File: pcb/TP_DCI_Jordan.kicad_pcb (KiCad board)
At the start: 2 copper layers, 50 x 30 mm, 19 parts, among them J1 MICRO, J2 Display, SW1 SW_DIP_x03, U1 PCF8574

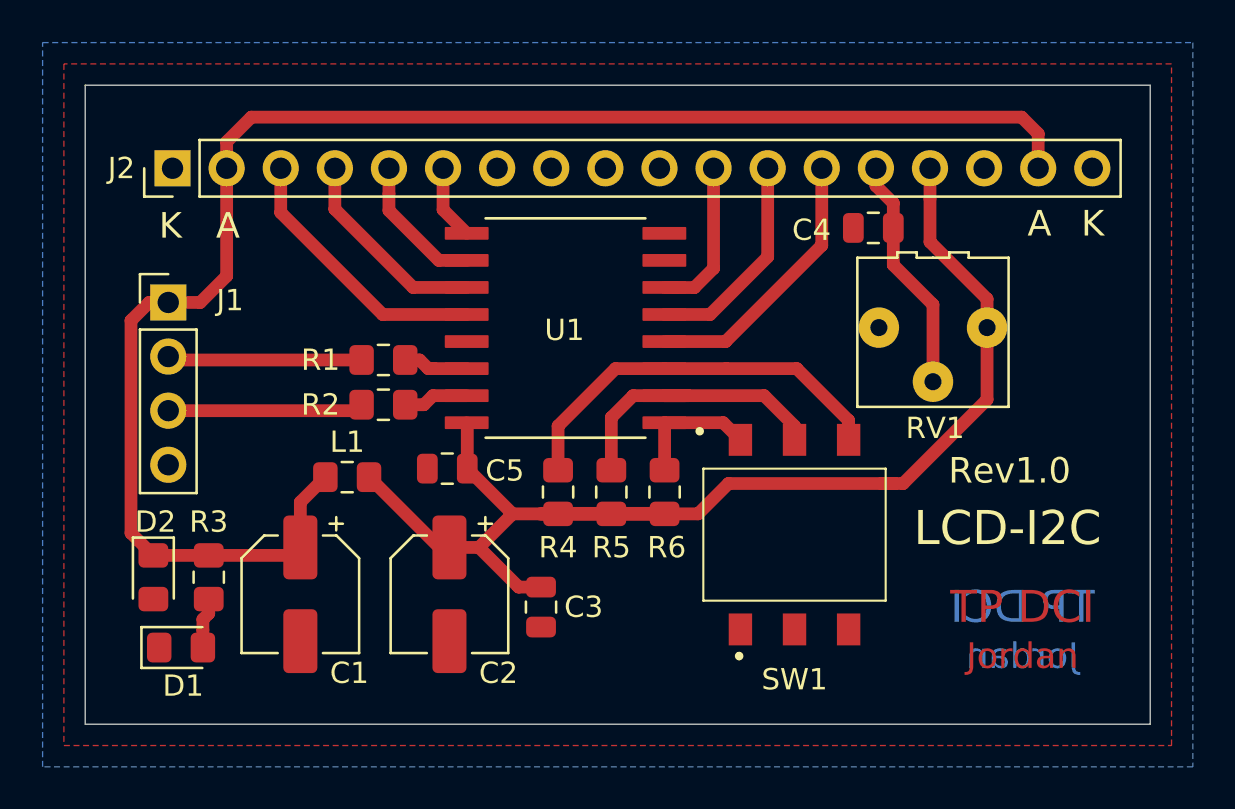
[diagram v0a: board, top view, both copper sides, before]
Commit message: actualización de KiCAD6.0
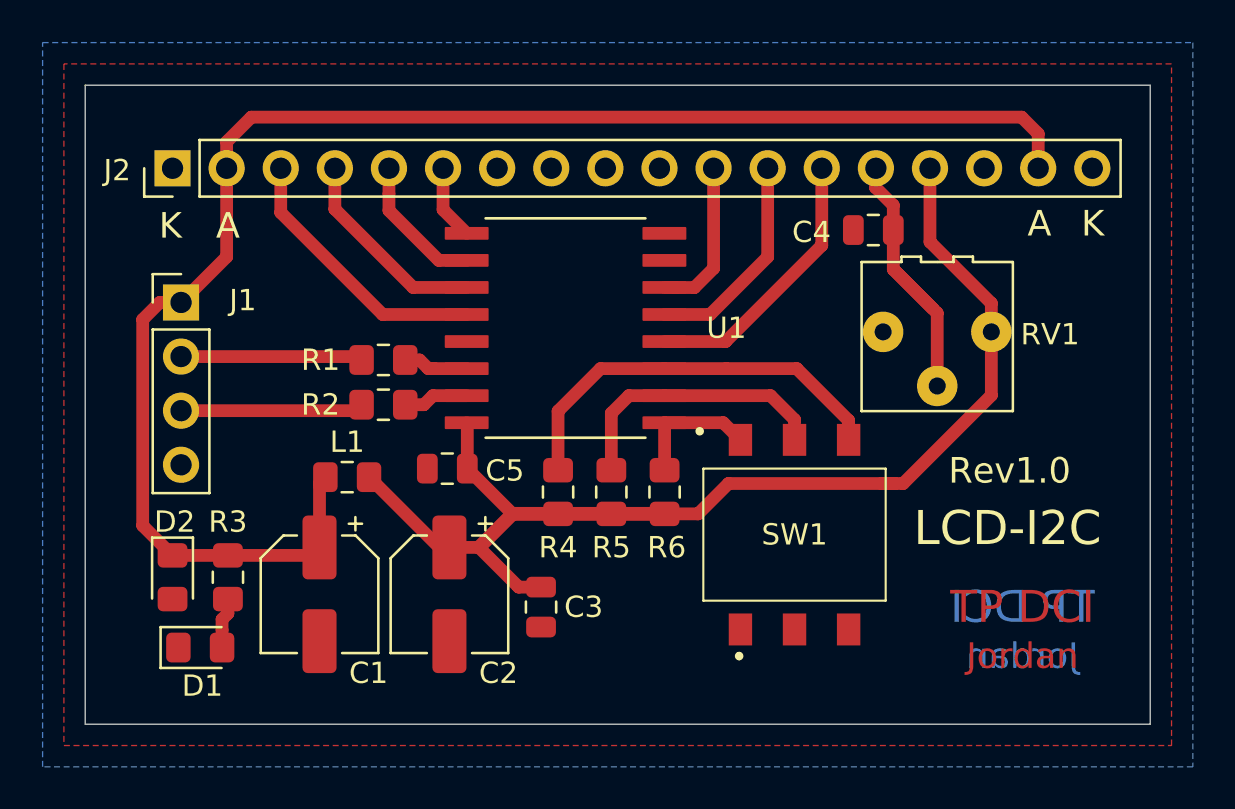
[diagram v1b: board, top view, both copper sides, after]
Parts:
- J2: value Display -> LCD16x2; footprint miConector:LCD_16x2_dosTipos -> DCI_Conector:LCD_16x2_dosTipos
- RV1: footprint miPotenciometro_RV09:miPote10k_3362P -> DCI_Pote:miPote10k_3362P
- SW1: footprint miConector:DIPSwitch_03 -> DCI_Switch:DIPSwitch_03
- U1: footprint miSMD:SOIC127P1030X265-16N -> DCI_PCF854:SOIC127P1030X265-16N
- moved C1 0.90 mm to (92.0, 133.9)
- moved D1 0.90 mm to (86.4, 136.4)
- moved R3 0.90 mm to (87.7, 133.1)
- moved D2 0.90 mm to (85.1, 133.1)
- moved J1 0.60 mm to (85.5, 120.2)
- moved RV1 0.28 mm to (121.0, 121.8)
- moved C4 0.10 mm to (118.0, 116.8)
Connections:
- R4 pad 1: Net-(R4-Pad1) -> Net-(U1-Pad3)
- R6 pad 1: Net-(R6-Pad1) -> Net-(U1-Pad1)
- SW1 pad 2: GND -> Net-(U1-Pad1)
- SW1 pad 4: Net-(R4-Pad1) -> Net-(R5-Pad1)
- SW1 pad 5: Net-(R5-Pad1) -> GND
- SW1 pad 6: Net-(R6-Pad1) -> Net-(U1-Pad3)
- U1 pad 1: Net-(R6-Pad1) -> Net-(U1-Pad1)
- U1 pad 13: Net-(U1-Pad13) -> unconnected-(U1-Pad13)
- U1 pad 3: Net-(R4-Pad1) -> Net-(U1-Pad3)
- U1 pad 7: Net-(U1-Pad7) -> unconnected-(U1-Pad7)
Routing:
- net Net-(U1-Pad3): track 0.00 -> 19.2 mm
- net Net-(R4-Pad1): track 18.7 -> 0.00 mm
- net Net-(R6-Pad1): track 6.15 -> 0.00 mm
- net Net-(U1-Pad1): track 0.00 -> 6.14 mm
- net /V0: track 11.7 -> 14.1 mm
- net /Vin: track 74.6 -> 73.2 mm
- net Net-(R5-Pad1): track 13.9 -> 13.0 mm
- net VDD: track 55.5 -> 54.8 mm
- net /SDA: track 9.19 -> 8.59 mm
- net /SCL: track 9.14 -> 8.54 mm
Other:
- net class Default removed

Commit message: maximizar espaciado entre conductores, IPC
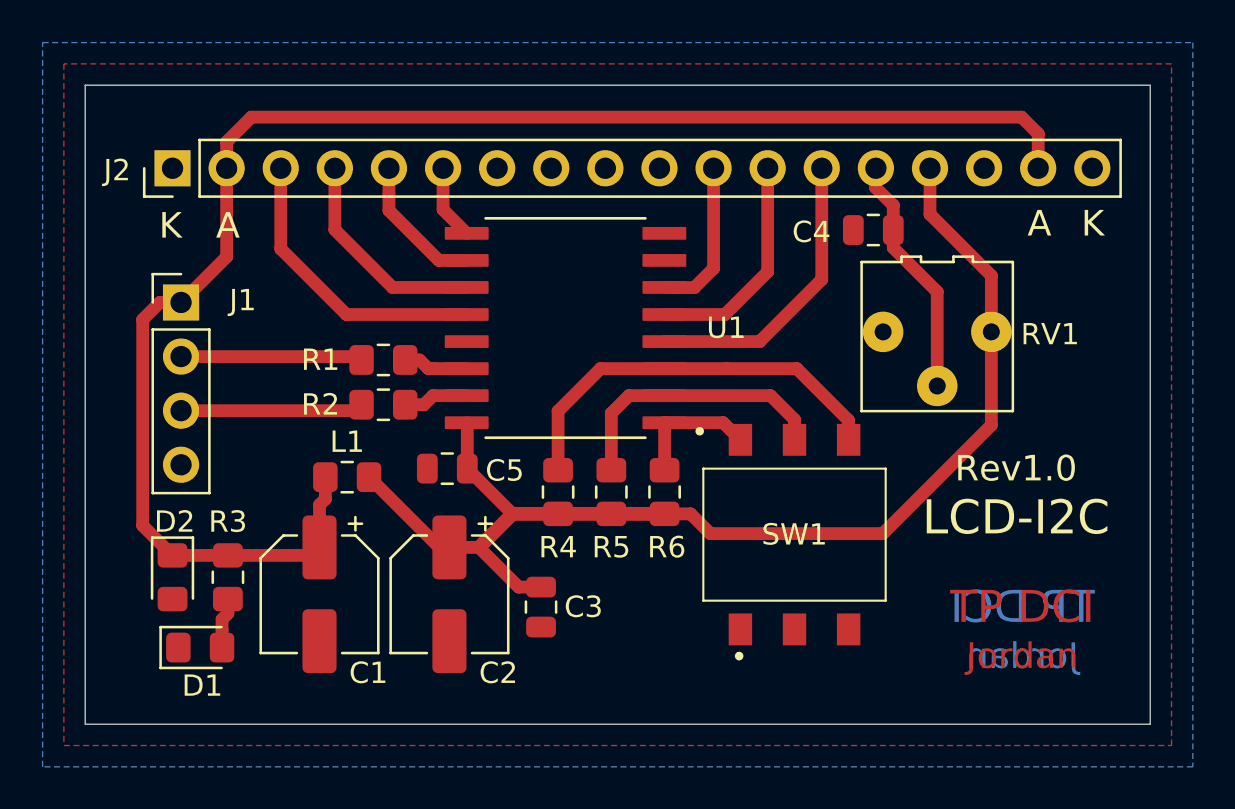
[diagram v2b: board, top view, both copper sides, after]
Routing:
- net /V0: track 14.1 -> 11.4 mm
- net /D7: track 12.8 -> 13.8 mm
- net VDD: track 54.8 -> 55.8 mm
- net /RS: track 12.9 -> 13.8 mm
- net /D6: track 9.63 -> 10.2 mm
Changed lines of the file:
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@@
     (effects (font (size 1.2 1.2) (thickness 0.2)))
   )
-  (gr_text "LCD-I2C" (at 124.3 130.8) (layer "F.SilkS")
+  (gr_text "LCD-I2C" (at 124.7 130.3) (layer "F.SilkS")
     (effects (font (size 1.6 1.6) (thickness 0.3)))
   )
-  (gr_text "Rev1.0" (at 124.4 128.1) (layer "F.SilkS")
+  (gr_text "Rev1.0" (at 124.7 128) (layer "F.SilkS")
     (effects (font (size 1.2 1.2) (thickness 0.2)))
   )
@@
   (segment (start 124.962081 111.5) (end 88.8 111.5) (width 0.6) (layer "F.Cu") (net 2))
   (segment (start 87.64 118.06) (end 87.64 113.9) (width 0.6) (layer "F.Cu") (net 2))
-  (segment (start 92 128.675) (end 92.275 128.4) (width 0.6) (layer "F.Cu") (net 2))
+  (segment (start 92.275 128.4) (end 92.275 129.425) (width 0.6) (layer "F.Cu") (net 2))
+  (segment (start 92 129.7) (end 92 131.7) (width 0.6) (layer "F.Cu") (net 2))
   (segment (start 87.64 113.9) (end 87.64 112.66) (width 0.6) (layer "F.Cu") (net 2))
   (segment (start 125.74 112.277919) (end 124.962081 111.5) (width 0.6) (layer "F.Cu") (net 2))
@@
   (segment (start 88.8 111.5) (end 87.64 112.66) (width 0.6) (layer "F.Cu") (net 2))
   (segment (start 83.7 121) (end 84.5 120.2) (width 0.6) (layer "F.Cu") (net 2))
-  (segment (start 92 131.7) (end 92 128.675) (width 0.6) (layer "F.Cu") (net 2))
+  (segment (start 92.275 129.425) (end 92 129.7) (width 0.6) (layer "F.Cu") (net 2))
   (segment (start 84.5 120.2) (end 85.5 120.2) (width 0.6) (layer "F.Cu") (net 2))
-  (segment (start 118.4 128.7) (end 111.2 128.7) (width 0.6) (layer "F.Cu") (net 3))
+  (segment (start 118.45 131.05) (end 123.54 125.96) (width 0.6) (layer "F.Cu") (net 3))
   (segment (start 99.4875 131.7) (end 98.1 131.7) (width 0.6) (layer "F.Cu") (net 3))
-  (segment (start 123.54 124.56) (end 119.4 128.7) (width 0.6) (layer "F.Cu") (net 3))
   (segment (start 98.9375 128) (end 98.9375 125.8725) (width 0.6) (layer "F.Cu") (net 3))
-  (segment (start 120.66 117.356498) (end 120.66 113.9) (width 0.6) (layer "F.Cu") (net 3))
+  (segment (start 123.54 121.58) (end 123.54 118.94) (width 0.6) (layer "F.Cu") (net 3))
+  (segment (start 109.425 130.125) (end 110.35 131.05) (width 0.6) (layer "F.Cu") (net 3))
+  (segment (start 108.2 130.125) (end 109.425 130.125) (width 0.6) (layer "F.Cu") (net 3))
+  (segment (start 123.54 121.58) (end 123.54 125.96) (width 0.6) (layer "F.Cu") (net 3))
   (segment (start 103.2 130.125) (end 101.0625 130.125) (width 0.65) (layer "F.Cu") (net 3))
-  (segment (start 119.4 128.7) (end 118.4 128.7) (width 0.6) (layer "F.Cu") (net 3))
-  (segment (start 123.54 121.58) (end 123.54 120.236498) (width 0.6) (layer "F.Cu") (net 3))
   (segment (start 105.7 130.125) (end 108.2 130.125) (width 0.65) (layer "F.Cu") (net 3))
   (segment (start 105.7 130.125) (end 103.2 130.125) (width 0.65) (layer "F.Cu") (net 3))
-  (segment (start 108.2 130.125) (end 109.775 130.125) (width 0.6) (layer "F.Cu") (net 3))
+  (segment (start 120.66 116.06) (end 120.66 113.9) (width 0.6) (layer "F.Cu") (net 3))
   (segment (start 98.9375 125.8725) (end 98.91 125.845) (width 0.6) (layer "F.Cu") (net 3))
   (segment (start 102.4 133.5625) (end 101.35 133.5625) (width 0.6) (layer "F.Cu") (net 3))
   (segment (start 98.9375 128) (end 101.0625 130.125) (width 0.6) (layer "F.Cu") (net 3))
-  (segment (start 111.2 128.7) (end 109.775 130.125) (width 0.6) (layer "F.Cu") (net 3))
   (segment (start 101.35 133.5625) (end 99.4875 131.7) (width 0.6) (layer "F.Cu") (net 3))
-  (segment (start 123.54 121.58) (end 123.54 124.56) (width 0.6) (layer "F.Cu") (net 3))
+  (segment (start 123.54 118.94) (end 120.66 116.06) (width 0.6) (layer "F.Cu") (net 3))
+  (segment (start 110.35 131.05) (end 118.45 131.05) (width 0.6) (layer "F.Cu") (net 3))
   (segment (start 97.625 131.7) (end 94.325 128.4) (width 0.6) (layer "F.Cu") (net 3))
   (segment (start 101.0625 130.125) (end 99.4875 131.7) (width 0.65) (layer "F.Cu") (net 3))
-  (segment (start 119 128.7) (end 118.4 128.7) (width 0.6) (layer "F.Cu") (net 3))
-  (segment (start 123.54 120.236498) (end 120.66 117.356498) (width 0.6) (layer "F.Cu") (net 3))
   (segment (start 98.1 131.7) (end 97.625 131.7) (width 0.6) (layer "F.Cu") (net 3))
   (segment (start 118.1 114.8) (end 118.9375 115.6375) (width 0.6) (layer "F.Cu") (net 4))
+  (segment (start 121 119.7) (end 118.9375 117.6375) (width 0.6) (layer "F.Cu") (net 4))
   (segment (start 118.12 113.9) (end 118.1 113.92) (width 0.6) (layer "F.Cu") (net 4))
-  (segment (start 118.9375 118.6375) (end 118.9375 116.8) (width 0.6) (layer "F.Cu") (net 4))
-  (segment (start 121 120.7) (end 118.9375 118.6375) (width 0.6) (layer "F.Cu") (net 4))
+  (segment (start 118.9375 117.6375) (end 118.9375 116.8) (width 0.6) (layer "F.Cu") (net 4))
   (segment (start 118.9375 115.6375) (end 118.9375 116.8) (width 0.6) (layer "F.Cu") (net 4))
-  (segment (start 120.8 120.5) (end 118.9375 118.6375) (width 0.6) (layer "F.Cu") (net 4))
+  (segment (start 121 124.12) (end 121 119.7) (width 0.6) (layer "F.Cu") (net 4))
   (segment (start 118.1 113.92) (end 118.1 114.8) (width 0.6) (layer "F.Cu") (net 4))
-  (segment (start 121 124.12) (end 121 120.7) (width 0.6) (layer "F.Cu") (net 4))
   (segment (start 93.815 122.74) (end 93.975 122.9) (width 0.6) (layer "F.Cu") (net 5))
   (segment (start 85.5 122.74) (end 93.815 122.74) (width 0.6) (layer "F.Cu") (net 5))
   (segment (start 85.5 125.28) (end 93.695 125.28) (width 0.6) (layer "F.Cu") (net 6))
   (segment (start 93.695 125.28) (end 93.975 125) (width 0.6) (layer "F.Cu") (net 6))
-  (segment (start 90.18 115.98) (end 90.18 113.9) (width 0.6) (layer "F.Cu") (net 7))
-  (segment (start 98.91 120.765) (end 94.965 120.765) (width 0.6) (layer "F.Cu") (net 7))
-  (segment (start 94.965 120.765) (end 90.18 115.98) (width 0.6) (layer "F.Cu") (net 7))
-  (segment (start 98.91 119.495) (end 96.395 119.495) (width 0.6) (layer "F.Cu") (net 8))
-  (segment (start 92.72 115.82) (end 92.72 113.9) (width 0.6) (layer "F.Cu") (net 8))
-  (segment (start 96.395 119.495) (end 92.72 115.82) (width 0.6) (layer "F.Cu") (net 8))
+  (segment (start 90.18 113.9) (end 90.18 117.68) (width 0.6) (layer "F.Cu") (net 7))
+  (segment (start 90.18 117.68) (end 93.265 120.765) (width 0.6) (layer "F.Cu") (net 7))
+  (segment (start 93.265 120.765) (end 98.91 120.765) (width 0.6) (layer "F.Cu") (net 7))
+  (segment (start 92.72 113.9) (end 92.72 116.785) (width 0.6) (layer "F.Cu") (net 8))
+  (segment (start 95.43 119.495) (end 92.72 116.785) (width 0.6) (layer "F.Cu") (net 8))
+  (segment (start 98.91 119.495) (end 95.43 119.495) (width 0.6) (layer "F.Cu") (net 8))
   (segment (start 97.601796 118.225) (end 95.26 115.883204) (width 0.6) (layer "F.Cu") (net 9))
   (segment (start 95.26 115.102081) (end 95.26 113.9) (width 0.6) (layer "F.Cu") (net 9))
@@
   (segment (start 110.5 118.6) (end 110.5 113.9) (width 0.6) (layer "F.Cu") (net 11))
   (segment (start 109.6 119.5) (end 110.5 118.6) (width 0.6) (layer "F.Cu") (net 11))
-  (segment (start 108.19 120.765) (end 110.335 120.765) (width 0.6) (layer "F.Cu") (net 12))
-  (segment (start 110.335 120.765) (end 113.04 118.06) (width 0.6) (layer "F.Cu") (net 12))
-  (segment (start 113.04 118.06) (end 113.04 113.9) (width 0.6) (layer "F.Cu") (net 12))
-  (segment (start 108.19 122.035) (end 111.065 122.035) (width 0.6) (layer "F.Cu") (net 13))
-  (segment (start 115.58 117.52) (end 115.58 113.9) (width 0.6) (layer "F.Cu") (net 13))
-  (segment (start 111.065 122.035) (end 115.58 117.52) (width 0.6) (layer "F.Cu") (net 13))
+  (segment (start 108.19 120.765) (end 111.035 120.765) (width 0.6) (layer "F.Cu") (net 12))
+  (segment (start 113.04 118.76) (end 113.04 113.9) (width 0.6) (layer "F.Cu") (net 12))
+  (segment (start 111.035 120.765) (end 113.04 118.76) (width 0.6) (layer "F.Cu") (net 12))
+  (segment (start 108.19 122.035) (end 112.665 122.035) (width 0.6) (layer "F.Cu") (net 13))
+  (segment (start 115.58 119.12) (end 115.58 113.9) (width 0.6) (layer "F.Cu") (net 13))
+  (segment (start 112.665 122.035) (end 115.58 119.12) (width 0.6) (layer "F.Cu") (net 13))
   (segment (start 87.7 134.125) (end 87.7 134.8) (width 0.6) (layer "F.Cu") (net 16))
   (segment (start 87.425 135.075) (end 87.425 135.575) (width 0.6) (layer "F.Cu") (net 16))

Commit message: presentación final
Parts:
- moved C4 0.10 mm to (118.1, 116.8)
- moved R1 0.10 mm to (94.9, 122.9)
- moved R2 0.10 mm to (94.9, 125.0)
